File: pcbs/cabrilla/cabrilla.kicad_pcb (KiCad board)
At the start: 2 copper layers, 150 x 78 mm, 50 parts, among them J1 hm_1, J10 Conn_01x06, J11 Conn_01x08, J12 Conn_01x10, J2 hm_2, J3 hm_3, J4 hm_4, J5 conector_entradas, J6 UART_LCD, J7 leds_velocidad, J8 UART_lora, J9 Conn_01x08, U1 lorabee, U2 LCD, U3 LoRa, U4 AZ1117-3.3, Y1 lcd, Y2 LoRa

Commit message: PCB
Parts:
- removed G***: LOGO, logos:hydro
- removed G***: LOGO, logos:id
- removed G***: LOGO, logos:un
- removed G***: LOGO, logos:solenium2
- removed JP1, JP2: jumper_con1, Connector_PinHeader_2.54mm:PinHeader_1x03_P2.54mm_Vertical
- removed STM1: u, arduino:STM32
- removed the U1 at (171.5, 103.0)
- added D1: 1N4148, Diode_SMD:D_SOD-323F, B.Cu at (98.0, 49.5)
- added J11: Conn_01x05, Connector_Molex:Molex_KK-254_AE-6410-05A_1x05_P2.54mm_Vertical, F.Cu at (112.5, 106.0)
- added K1: G5V-1, Relay_THT:Relay_SPDT_Omron_G5V-1, F.Cu at (95.5, 44.5)
- added Q1: PN2222A, Package_TO_SOT_SMD:SOT-23_Handsoldering, B.Cu at (106.5, 50.5)
- added R13: 10k, Resistor_SMD:R_0805_2012Metric_Pad1.15x1.40mm_HandSolder, B.Cu at (105.5, 44.5)
- added R14: 10k, Resistor_SMD:R_0805_2012Metric_Pad1.15x1.40mm_HandSolder, F.Cu at (122.5, 44.5)
- added R15: 10k, Resistor_SMD:R_0805_2012Metric_Pad1.15x1.40mm_HandSolder, F.Cu at (188.0, 53.5)
- added SW1: SW_Push, Button_Switch_SMD:SW_Push_1P1T_NO_6x6mm_H9.5mm, F.Cu at (165.0, 45.0)
- added SW2: SW_Push, Button_Switch_SMD:SW_Push_1P1T_NO_6x6mm_H9.5mm, F.Cu at (180.1, 55.8)
- added U2: STM32, elementos:STM32, F.Cu at (130.5, 53.5)
- added U3: lorabee, elementos:lorabee, F.Cu at (182.5, 70.0)
- 3V1: renamed from 3V3; footprint LED_SMD:LED_0805_2012Metric -> LED_SMD:LED_0805_2012Metric_Pad1.15x1.40mm_HandSolder
- 5V1: footprint LED_SMD:LED_0805_2012Metric -> LED_SMD:LED_0805_2012Metric_Pad1.15x1.40mm_HandSolder
- C2: renamed from C6; footprint Capacitor_SMD:C_0805_2012Metric -> Capacitor_SMD:C_0805_2012Metric_Pad1.15x1.40mm_HandSolder; moved to B.Cu
- C3: renamed from C7; footprint Capacitor_SMD:C_0805_2012Metric -> Capacitor_SMD:C_0805_2012Metric_Pad1.15x1.40mm_HandSolder; moved to B.Cu
- C4: renamed from C2; footprint Capacitor_SMD:C_0805_2012Metric -> Capacitor_SMD:C_0805_2012Metric_Pad1.15x1.40mm_HandSolder
- C5: renamed from C3; footprint Capacitor_SMD:C_0805_2012Metric -> Capacitor_SMD:C_0805_2012Metric_Pad1.15x1.40mm_HandSolder
- C6: renamed from C4; footprint Capacitor_SMD:C_0805_2012Metric -> Capacitor_SMD:C_0805_2012Metric_Pad1.15x1.40mm_HandSolder
- C7: renamed from C5; footprint Capacitor_SMD:C_0805_2012Metric -> Capacitor_SMD:C_0805_2012Metric_Pad1.15x1.40mm_HandSolder
- R1: renamed from R5; footprint Resistor_SMD:R_0805_2012Metric -> Resistor_SMD:R_0805_2012Metric_Pad1.15x1.40mm_HandSolder
- R2: renamed from R8; footprint Resistor_SMD:R_0805_2012Metric -> Resistor_SMD:R_0805_2012Metric_Pad1.15x1.40mm_HandSolder
- U1: renamed from U4; moved to B.Cu
- moved deb_lcd1 118.5 mm to (90.0, 108.9)
- moved C1 101.0 mm to (195.5, 46.5)
- moved 3V1 66.1 mm to (183.0, 43.5)
- moved R2 66.1 mm to (187.4, 43.5)
- moved C5 59.6 mm to (154.4, 84.5)
- moved C4 52.9 mm to (154.5, 79.5), turned to 180 degrees
- moved R3 47.7 mm to (172.0, 99.0), turned to 270 degrees
- moved Y1 41.5 mm to (159.8, 84.4), turned to 90 degrees
- moved R4 40.7 mm to (177.0, 99.0), turned to 270 degrees
- moved deb_com1 34.7 mm to (98.0, 109.0)
- moved R5 33.7 mm to (182.0, 99.0), turned to 270 degrees
- moved C3 30.0 mm to (78.6, 46.0), turned to 180 degrees
- moved C2 29.7 mm to (78.6, 43.7), turned to 180 degrees
- moved C6 28.1 mm to (95.0, 79.5)
- moved R6 26.1 mm to (187.5, 99.0), turned to 90 degrees
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- renumbered U3 to COM1, J7 to J1, J12 to J10, J1 to J2, J2 to J3, J3 to J4, J4 to J5, J5 to J6, J9 to J7, J10 to J8, J11 to J9, U2 to LCD1, R2 to R10, R3 to R11, R4 to R12, R6 to R3, R7 to R4, 1k1 to R5, 1k2 to R6, 1k3 to R7, 1k4 to R8, R1 to R9, J8 to deb_com1, J6 to deb_lcd1
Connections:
- net Net-(J5-Pad12) renamed /motor_h
- net Net-(J5-Pad9) renamed /freno
- COM1 pad 16: Net-(U3-Pad16) -> /Arduino LoRa/SS_lora
- COM1 pad 17: Net-(U3-Pad17) -> /Arduino LoRa/MOSI
- COM1 pad 18: Net-(U3-Pad18) -> /Arduino LoRa/MISO
- COM1 pad 19: Net-(U3-Pad19) -> /Arduino LoRa/SCK
- COM1 pad 2: /Arduino LoRa/rx_lora -> /tx_com
- COM1 pad 3: /Arduino LoRa/tx_lora -> /rx_com
- J2 pad 1: +5V -> +3V3
- J3 pad 1: +5V -> +3V3
- J4 pad 1: +5V -> +3V3
- J5 pad 1: +5V -> +3V3
- J6 pad 10: /com_1 -> Net-(J6-Pad10)
- J6 pad 11: /com_2 -> /motor_l
- J6 pad 2: +5V -> /vin
- J6 pad 7: /hm -> /pwm_motor
- J6 pad 8: /motor_out -> /reversa
- LCD1 pad 2: /Arduino LCD/rx_lcd -> /rx_lcd
- LCD1 pad 3: /Arduino LCD/tx_lcd -> /tx_lcd
- deb_com1 pad 2: /Arduino LoRa/tx_lora -> /tx_com
- deb_com1 pad 3: /Arduino LoRa/rx_lora -> /rx_com
- deb_lcd1 pad 2: /Arduino LCD/tx_lcd -> /rx_lcd
- deb_lcd1 pad 3: /Arduino LCD/rx_lcd -> /tx_lcd
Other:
- board text added: "gnd"
- board text added: "rx"
- board text added: "tx"

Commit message: ixed
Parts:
- D1: value 1N4148 -> 1N4007; footprint Diode_SMD:D_SOD-323F -> Diode_SMD:D_SMB
- J11: value Conn_01x05 -> Conn_analogo
- Q1: value PN2222A -> Q_NPN_BEC; moved to F.Cu
- R1, R2, R3, R4: value 1k -> 120
- R10, R11, R12, R9: moved to B.Cu
- R5, R6, R7, R8: value 330 -> 120
- Y1: footprint Crystal:Crystal_HC49-4H_Vertical -> Crystal:Crystal_SMD_HC49-SD_HandSoldering
- Y2: footprint Crystal:Crystal_HC49-4H_Vertical -> Crystal:Crystal_SMD_HC49-SD
- moved H1 143.1 mm to (105.5, 59.5)
- moved J3 135.7 mm to (206.5, 88.0), turned to 270 degrees
- moved J4 135.7 mm to (206.5, 80.0), turned to 270 degrees
- moved J2 135.5 mm to (206.5, 62.5), turned to 270 degrees
- moved J5 135.5 mm to (206.5, 72.0), turned to 270 degrees
- moved R10 124.5 mm to (202.5, 91.5), turned to 90 degrees
- moved R11 124.5 mm to (202.5, 83.5), turned to 90 degrees
- moved R12 124.5 mm to (202.5, 75.5), turned to 90 degrees
- moved R9 124.5 mm to (202.5, 66.0), turned to 90 degrees
- moved H2 116.0 mm to (105.5, 99.0)
- moved U3 110.1 mm to (72.5, 73.5)
- moved H4 55.2 mm to (193.0, 59.5)
- moved SW1 49.2 mm to (116.5, 53.0), turned to 180 degrees
- moved H3 36.6 mm to (193.0, 90.5)
- moved SW2 11.5 mm to (169.0, 53.0), turned to 180 degrees
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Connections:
- J6 pad 2: /vin -> +5V
- Q1 pad 1: GND -> Net-(Q1-Pad1)
- Q1 pad 2: Net-(Q1-Pad2) -> GND
- R13 pad 1: Net-(Q1-Pad2) -> Net-(Q1-Pad1)
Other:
- board text added: "Diseñó: Diego Fernando Uribe Revisó: Rev: 1.0 Hydrómetra - E&C Hecho en Colombia"
- board text removed: "Hombre muerto"

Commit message: Added Hydrómetra logo
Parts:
- added G***: LOGO, logos:hydro, F.Cu at (139.0, 43.5)

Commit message: 80
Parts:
- removed G***: LOGO, logos:hydro
- added C8: 100uF, Capacitor_SMD:CP_Elec_8x6.2, B.Cu at (154.0, 64.0)
- added D2: 1N4148, Diode_SMD:D_SOD-323_HandSoldering, F.Cu at (84.5, 53.0)
- added F1: 1A, Fuse:Fuse_2816_7142Metric_Pad3.20x4.45mm_HandSolder, F.Cu at (196.5, 77.5)
- added J12: inputs, Connector_Molex:Molex_KK-254_AE-6410-08A_1x08_P2.54mm_Vertical, F.Cu at (138.0, 85.5)
- added K2: G5V-1, Relay_THT:Relay_SPDT_Omron_G5V-1, F.Cu at (73.4, 52.3)
- added Power1: Conn_01x03, Connector_PinHeader_2.54mm:PinHeader_1x03_P2.54mm_Vertical, F.Cu at (97.0, 109.0)
- added Q2: Q_NPN_BEC, Package_TO_SOT_SMD:SOT-23_Handsoldering, F.Cu at (83.5, 58.0)
- added R16: 390, Resistor_SMD:R_0805_2012Metric_Pad1.15x1.40mm_HandSolder, B.Cu at (150.5, 68.5)
- added R17: 10k, Resistor_SMD:R_0805_2012Metric_Pad1.15x1.40mm_HandSolder, F.Cu at (91.0, 51.7)
- D1: value 1N4007 -> 1N4148; footprint Diode_SMD:D_SMB -> Diode_SMD:D_SOD-323_HandSoldering
- J6: value conector_entradas -> Conn_analogo; footprint Connector_Molex:Molex_KK-254_AE-6410-12A_1x12_P2.54mm_Vertical -> Connector_Molex:Molex_KK-254_AE-6410-05A_1x05_P2.54mm_Vertical; moved to F.Cu
- R1, R2: value 120 -> 1k
- R3, R4, R5, R6, R7, R8: value 120 -> 10k
- Y2: footprint Crystal:Crystal_SMD_HC49-SD -> Crystal:Crystal_SMD_HC49-SD_HandSoldering
- moved J6 42.3 mm to (179.1, 78.4), turned to 0 degrees
- moved deb_com1 10.0 mm to (88.0, 109.0)
- moved deb_lcd1 9.00 mm to (81.0, 108.9)
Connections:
- net /Arduino LCD/osc_1 renamed /LCD/osc_1
- net /Arduino LCD/osc_2 renamed /LCD/osc_2
- net /Arduino LoRa/MISO renamed /Comunicaciones/MISO
- net /Arduino LoRa/MOSI renamed /Comunicaciones/MOSI
- net /Arduino LoRa/SCK renamed /Comunicaciones/SCK
- net /Arduino LoRa/SS_lora renamed /Comunicaciones/SS_lora
- net /Arduino LoRa/osc_1 renamed /Comunicaciones/osc_1
- net /Arduino LoRa/osc_2 renamed /Comunicaciones/osc_2
- net /bms_l renamed Net-(J6-Pad5)
- COM1 pad 2: /tx_com -> /Comunicaciones/rx_lora
- COM1 pad 3: /rx_com -> /Comunicaciones/tx_lora
- J6 pad 2: +5V -> +3V3
- J6 pad 3: Net-(J6-Pad3) -> /analog_x2
- J6 pad 4: /bms_h -> /analog_y2
- J8 pad 1: Net-(J8-Pad1) -> /LCD/RD
- J8 pad 2: Net-(J8-Pad2) -> /LCD/WR
- J8 pad 3: Net-(J8-Pad3) -> /LCD/RS
- J8 pad 4: Net-(J8-Pad4) -> /LCD/CS
- J8 pad 5: Net-(J8-Pad5) -> /LCD/RST
- LCD1 pad 2: /rx_lcd -> /LCD/rx_lcd
- LCD1 pad 23: Net-(LCD1-Pad23) -> /LCD/RD
- LCD1 pad 24: Net-(LCD1-Pad24) -> /LCD/WR
- LCD1 pad 25: Net-(LCD1-Pad25) -> /LCD/RS
- LCD1 pad 26: Net-(LCD1-Pad26) -> /LCD/CS
- LCD1 pad 27: Net-(LCD1-Pad27) -> /LCD/RST
- LCD1 pad 3: /tx_lcd -> /LCD/tx_lcd
- U2 pad 1: Net-(U2-Pad1) -> /led_m1
- U2 pad 10: Net-(U2-Pad10) -> /hm_2
- U2 pad 11: Net-(U2-Pad11) -> /hm_1
- U2 pad 14: Net-(U2-Pad14) -> /freno_signal
- U2 pad 15: Net-(U2-Pad15) -> /led_m5
- U2 pad 16: Net-(U2-Pad16) -> /led_m6
- U2 pad 2: Net-(U2-Pad2) -> /led_m2
- U2 pad 25: /hm_4 -> Net-(U2-Pad25)
- U2 pad 26: /hm_3 -> Net-(U2-Pad26)
- U2 pad 27: /tx_lcd -> /LCD/rx_lcd
- U2 pad 28: /rx_lcd -> /LCD/tx_lcd
- U2 pad 29: /hm_2 -> /corriente
- U2 pad 3: Net-(U2-Pad3) -> /led_m3
- U2 pad 30: /hm_1 -> /analog_x2
- U2 pad 31: /analog_x -> /analog_y2
- U2 pad 32: /analog_y -> /analog_x
- U2 pad 33: Net-(U2-Pad33) -> /analog_y
- U2 pad 34: /pwm_motor -> Net-(R16-Pad2)
- U2 pad 4: Net-(U2-Pad4) -> /led_m4
- U2 pad 6: /rx_com -> /Comunicaciones/rx_lora
- U2 pad 7: /tx_com -> /Comunicaciones/tx_lora
- U2 pad 8: Net-(U2-Pad8) -> /hm_4
- U2 pad 9: Net-(U2-Pad9) -> /hm_3
- deb_com1 pad 2: /tx_com -> /Comunicaciones/tx_lora
- deb_com1 pad 3: /rx_com -> /Comunicaciones/rx_lora
- deb_lcd1 pad 2: /rx_lcd -> /LCD/tx_lcd
- deb_lcd1 pad 3: /tx_lcd -> /LCD/rx_lcd
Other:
- board text added: "3v3"
- board text added: "5V"
- board text added: "Debug"

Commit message: Updated footprints
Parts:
- C1, C8: footprint Capacitor_SMD:CP_Elec_8x6.2 -> Capacitor_SMD:CP_Elec_8x10
- F1: footprint Fuse:Fuse_2816_7142Metric_Pad3.20x4.45mm_HandSolder -> Fuse:Fuse_0201_0603Metric
- Y1, Y2: footprint Crystal:Crystal_SMD_HC49-SD_HandSoldering -> Crystal:Crystal_HC49-4H_Vertical
- moved U1 30.6 mm to (104.1, 69.8)
- moved R16 5.18 mm to (153.9, 72.4)
- moved 5V1 4.18 mm to (85.1, 43.2)
- moved C8 2.21 mm to (156.2, 64.0)
- moved R11 1.97 mm to (200.7, 82.8)
- moved R10 1.84 mm to (200.7, 91.4)
- moved R9 1.84 mm to (200.7, 66.0)
- moved R12 1.84 mm to (200.7, 75.5)
- moved R1 1.80 mm to (87.7, 47.2)

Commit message: Routed
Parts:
- removed J1: leds_velocidad, Connector_Molex:Molex_KK-254_AE-6410-12A_1x12_P2.54mm_Vertical
- removed J10: Conn_01x10, Connector_Molex:Molex_KK-254_AE-6410-10A_1x10_P2.54mm_Vertical
- removed R5, R6: 10k, Resistor_SMD:R_0805_2012Metric_Pad1.15x1.40mm_HandSolder
- added lcd_power1: lcd_power, Connector_Molex:Molex_KK-254_AE-6410-08A_1x08_P2.54mm_Vertical, F.Cu at (139.5, 114.0)
- added leds1: Conn_01x04, Connector_Molex:Molex_KK-254_AE-6410-04A_1x04_P2.54mm_Vertical, F.Cu at (111.5, 44.5)
- added leds2: Conn_01x04, Connector_Molex:Molex_KK-254_AE-6410-04A_1x04_P2.54mm_Vertical, F.Cu at (98.0, 44.5)
- C2, C3, R13: moved to F.Cu
- D2, J12, R3, R4, R7, R8: moved to B.Cu
- F1: footprint Fuse:Fuse_0201_0603Metric -> Fuse:Fuse_2816_7142Metric_Pad3.20x4.45mm_HandSolder; moved to B.Cu
- J9: value Conn_01x08 -> lcd_digital1
- SW1, SW2: footprint Button_Switch_SMD:SW_Push_1P1T_NO_6x6mm_H9.5mm -> Button_Switch_SMD:SW_Push_1P1T_NO_CK_KSC6xxJ
- moved 5V1 134.7 mm to (199.0, 115.0), turned to 180 degrees
- moved R1 126.1 mm to (194.0, 115.0), turned to 180 degrees
- moved R8 107.1 mm to (100.5, 53.5), turned to 90 degrees
- moved hm4 105.0 mm to (110.0, 113.5), turned to 180 degrees
- moved R12 99.8 mm to (106.5, 108.5), turned to 0 degrees
- moved R7 98.1 mm to (105.6, 53.5), turned to 90 degrees
- moved hm3 95.6 mm to (117.0, 113.5), turned to 180 degrees
- moved C1 94.2 mm to (120.5, 103.5), turned to 180 degrees
- moved hm1 91.1 mm to (131.0, 113.5), turned to 180 degrees
- moved R11 90.9 mm to (113.5, 108.5), turned to 0 degrees
- moved C2 90.3 mm to (142.0, 108.0), turned to 0 degrees
- moved hm2 86.4 mm to (124.0, 113.5), turned to 180 degrees
- moved C3 85.5 mm to (137.5, 108.0)
- moved R9 84.6 mm to (127.5, 108.5), turned to 0 degrees
- moved R10 82.0 mm to (120.5, 108.5), turned to 0 degrees
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- renumbered J11 to analogo1, J6 to analogo2, J2 to hm1, J3 to hm2, J4 to hm3, J5 to hm4, J8 to lcd_analog1, J7 to lcd_digital2
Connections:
- net Net-(R16-Pad2) renamed /raw_pwm
- COM1 pad 11: Net-(COM1-Pad11) -> /Comunicaciones/RESET
- COM1 pad 4: Net-(COM1-Pad4) -> /Comunicaciones/DIO0
- F1 pad 2: +5V -> VCC
- J12 pad 2: +5V -> Net-(J12-Pad2)
- J12 pad 3: /corriente -> /pwm_motor
- J12 pad 4: /pwm_motor -> /freno
- J12 pad 6: /freno -> /corriente
- J12 pad 8: Net-(J12-Pad8) -> VCC
- J9 pad 3: Net-(J9-Pad3) -> /LCD/D2
- J9 pad 4: Net-(J9-Pad4) -> /LCD/D3
- J9 pad 5: Net-(J9-Pad5) -> /LCD/D4
- J9 pad 6: Net-(J9-Pad6) -> /LCD/D5
- J9 pad 7: Net-(J9-Pad7) -> /LCD/D6
- J9 pad 8: Net-(J9-Pad8) -> /LCD/D7
- LCD1 pad 11: Net-(LCD1-Pad11) -> /LCD/D5
- LCD1 pad 12: Net-(LCD1-Pad12) -> /LCD/D6
- LCD1 pad 13: Net-(LCD1-Pad13) -> /LCD/D7
- LCD1 pad 14: Net-(LCD1-Pad14) -> /LCD/D0
- LCD1 pad 15: Net-(LCD1-Pad15) -> /LCD/D1
- LCD1 pad 16: Net-(LCD1-Pad16) -> /LCD/SS
- LCD1 pad 17: Net-(LCD1-Pad17) -> /LCD/DI
- LCD1 pad 18: Net-(LCD1-Pad18) -> /LCD/DO
- LCD1 pad 19: Net-(LCD1-Pad19) -> /LCD/SCK
- LCD1 pad 22: Net-(LCD1-Pad22) -> GND
- LCD1 pad 4: Net-(LCD1-Pad4) -> /LCD/D2
- LCD1 pad 5: Net-(LCD1-Pad5) -> /LCD/D3
- LCD1 pad 6: Net-(LCD1-Pad6) -> /LCD/D4
- LCD1 pad 8: Net-(LCD1-Pad22) -> GND
- R7 pad 1: /led_m5 -> /led_m3
- R8 pad 1: /led_m6 -> /led_m4
- U2 pad 10: /hm_2 -> /reversa_signal
- U2 pad 11: /hm_1 -> /freno_signal
- U2 pad 13: /reversa_signal -> Net-(U2-Pad13)
- U2 pad 14: /freno_signal -> /hm_4
- U2 pad 15: /led_m5 -> /hm_3
- U2 pad 16: /led_m6 -> /hm_2
- U2 pad 17: Net-(U2-Pad17) -> /hm_1
- U2 pad 8: /hm_4 -> Net-(U2-Pad8)
- U2 pad 9: /hm_3 -> Net-(U2-Pad9)
- U3 pad 12: Net-(U3-Pad12) -> /Comunicaciones/DIO0
- U3 pad 5: Net-(U3-Pad5) -> /Comunicaciones/RESET
- analogo1 pad 3: /analog_x -> /analog_y
- analogo1 pad 4: /analog_y -> /analog_x
- lcd_analog1 pad 1: /LCD/RD -> /LCD/RST
- lcd_analog1 pad 2: /LCD/WR -> /LCD/CS
- lcd_analog1 pad 4: /LCD/CS -> /LCD/WR
- lcd_analog1 pad 5: /LCD/RST -> /LCD/RD
- lcd_digital2 pad 3: Net-(J7-Pad3) -> /LCD/SCK
- lcd_digital2 pad 4: Net-(J7-Pad4) -> /LCD/DO
- lcd_digital2 pad 5: Net-(J7-Pad5) -> /LCD/DI
- lcd_digital2 pad 6: Net-(J7-Pad6) -> /LCD/SS
- lcd_digital2 pad 7: Net-(J7-Pad7) -> /LCD/D1
- lcd_digital2 pad 8: Net-(J7-Pad8) -> /LCD/D0
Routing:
- net +3V3: track 0.00 -> 325.7 mm, vias 0 -> 8
- net +5V: track 0.00 -> 256.7 mm, vias 0 -> 6
- net /reversa_signal: track 0.00 -> 182.3 mm, vias 0 -> 4
- net /LCD/rx_lcd: track 0.00 -> 122.0 mm, vias 0 -> 6
- net /LCD/tx_lcd: track 0.00 -> 115.4 mm, vias 0 -> 1
- net /reversa: track 0.00 -> 78.5 mm
- net /freno: track 0.00 -> 77.0 mm
- net /Comunicaciones/rx_lora: track 0.00 -> 74.6 mm, vias 0 -> 2
- net /LCD/D2: track 0.00 -> 72.8 mm, vias 0 -> 1
- net /Comunicaciones/tx_lora: track 0.00 -> 71.4 mm, vias 0 -> 1
- net /LCD/D3: track 0.00 -> 70.2 mm, vias 0 -> 1
- net /freno_signal: track 0.00 -> 64.8 mm, vias 0 -> 6
- net /LCD/WR: track 0.00 -> 62.8 mm
- net /LCD/RS: track 0.00 -> 61.5 mm
- net /LCD/D4: track 0.00 -> 59.1 mm
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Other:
- net class Default: trace_width 0.25 -> 0.8
- net class entrada added: clearance 0.2, trace_width 1, via_dia 0.8, via_drill 0.4

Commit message: Final
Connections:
- J12 pad 2: Net-(J12-Pad2) -> GND
- J12 pad 7: Net-(J12-Pad7) -> GND
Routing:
- net /LCD/D0: track 0.00 -> 76.3 mm, vias 0 -> 4
- net /LCD/tx_lcd: track 115.4 -> 189.3 mm, vias 1 -> 6
- net +3V3: track 325.7 -> 374.5 mm, vias 8 -> 9
- net GND: track 0.00 -> 38.5 mm, vias 0 -> 33
- net +5V: track 256.7 -> 252.7 mm
- net /reversa_signal: vias 4 -> 3
- added copper zone on B.Cu, net GND
- added copper zone on F.Cu, net GND

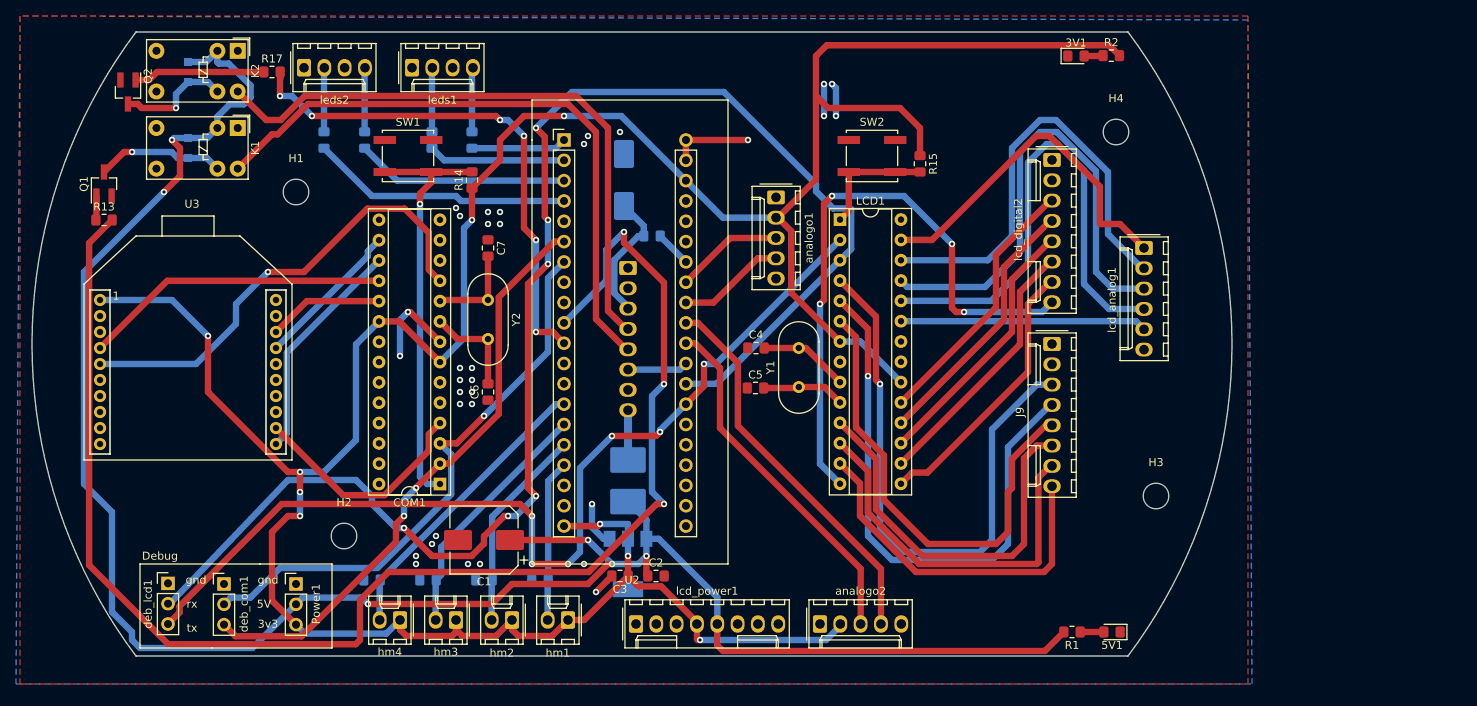
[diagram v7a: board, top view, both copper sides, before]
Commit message: Cambiados los parámetros de rutero
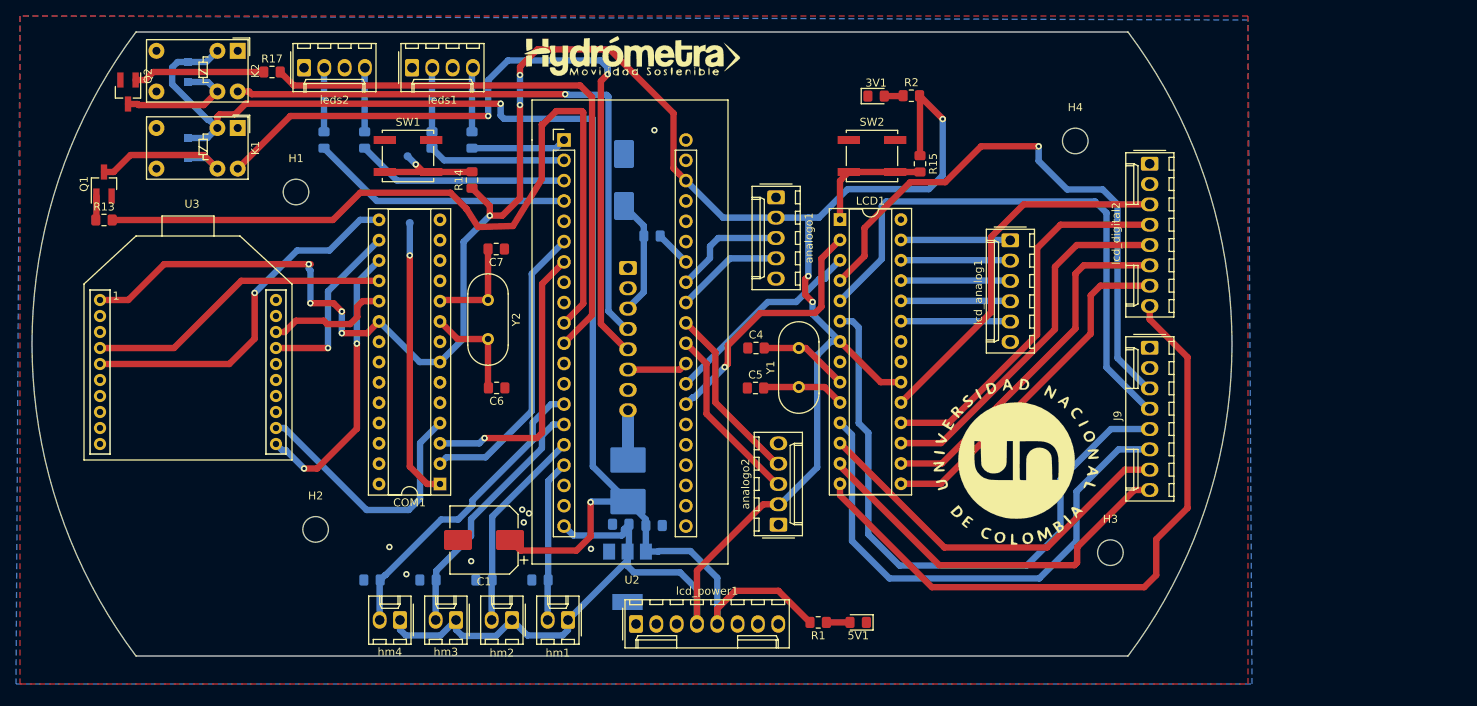
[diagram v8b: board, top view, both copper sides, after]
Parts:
- removed Power1: Conn_01x03, Connector_PinHeader_2.54mm:PinHeader_1x03_P2.54mm_Vertical
- removed deb_com1: UART_lora, Connector_PinHeader_2.54mm:PinHeader_1x03_P2.54mm_Vertical
- removed deb_lcd1: UART_LCD, Connector_PinHeader_2.54mm:PinHeader_1x03_P2.54mm_Vertical
- added G***: LOGO, logos:id, B.Cu at (84.2, 82.1)
- added G***: LOGO, logos:solenium2, B.Cu at (89.3, 110.1)
- added G***: LOGO, logos:un, F.Cu at (187.0, 93.2)
- added G***: LOGO, logos:hydro, F.Cu at (139.0, 43.0)
- added REF**: TestPoint_Pad_D1.0mm, TestPoint:TestPoint_Pad_D1.0mm, B.Cu at (111.2, 63.9)
- added REF**: TestPoint_Pad_D1.0mm, TestPoint:TestPoint_Pad_D1.0mm, B.Cu at (111.0, 55.5)
- C2, C3: moved to B.Cu
- moved 5V1 31.7 mm to (167.3, 113.8)
- moved R1 31.7 mm to (162.3, 113.8)
- moved 3V1 25.5 mm to (169.5, 48.0)
- moved R2 25.5 mm to (173.9, 48.0)
- moved lcd_analog1 16.7 mm to (186.3, 66.0)
- moved analogo2 13.5 mm to (157.3, 101.6), turned to 90 degrees
- moved J9 12.2 mm to (203.7, 79.5)
- moved lcd_digital2 12.2 mm to (203.7, 56.5)
- moved H3 9.09 mm to (198.8, 105.1)
- moved C3 6.47 mm to (137.6, 101.5)
- moved C2 6.31 mm to (141.8, 101.7)
- moved H4 5.21 mm to (194.4, 53.6)
- moved H2 3.64 mm to (99.5, 102.2)
- moved U1 1.60 mm to (138.4, 108.1)
- moved C6 1.19 mm to (122.1, 84.5), turned to 180 degrees
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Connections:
- net Net-(COM1-Pad1) renamed /Comunicaciones/arst
- COM1 pad 11: /Comunicaciones/RESET -> Net-(COM1-Pad11)
- COM1 pad 15: Net-(COM1-Pad15) -> /Comunicaciones/RESET
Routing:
- net /LCD/tx_lcd: track 189.3 -> 26.4 mm, vias 6 -> 0
- net /LCD/rx_lcd: track 122.0 -> 32.6 mm, vias 6 -> 1
- net /reversa_signal: track 182.3 -> 100.6 mm, vias 3 -> 0
- net +5V: track 252.7 -> 180.7 mm, vias 6 -> 2
- net /LCD/WR: track 62.8 -> 13.7 mm
- net /LCD/RS: track 61.5 -> 13.7 mm
- net +3V3: track 374.5 -> 329.4 mm, vias 9 -> 10
- net /LCD/CS: track 56.3 -> 13.7 mm
- net GND: track 38.5 -> 0.00 mm, vias 33 -> 8
- net /Comunicaciones/rx_lora: track 74.6 -> 37.1 mm, vias 2 -> 0
- net /Comunicaciones/tx_lora: track 71.4 -> 35.8 mm
- net /LCD/RST: track 44.3 -> 13.7 mm
- net /analog_y2: track 48.6 -> 22.5 mm
- net /analog_x2: track 44.8 -> 22.5 mm
- net /LCD/D4: track 59.1 -> 76.7 mm
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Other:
- net class Default: clearance 0.2 -> 0.3
- net class entrada: clearance 0.2 -> 0.3; trace_width 1 -> 1.5
- rule trace_clearance: 0.2 -> 0.3
- board text removed: "3v3"
- board text removed: "5V"
- board text removed: "Debug"
- board text removed: "gnd"
- board text removed: "rx"
- board text removed: "tx"
